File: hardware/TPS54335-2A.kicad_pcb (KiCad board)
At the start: 2 copper layers, 17 parts, among them J1 header, U1 TPS54335-2A

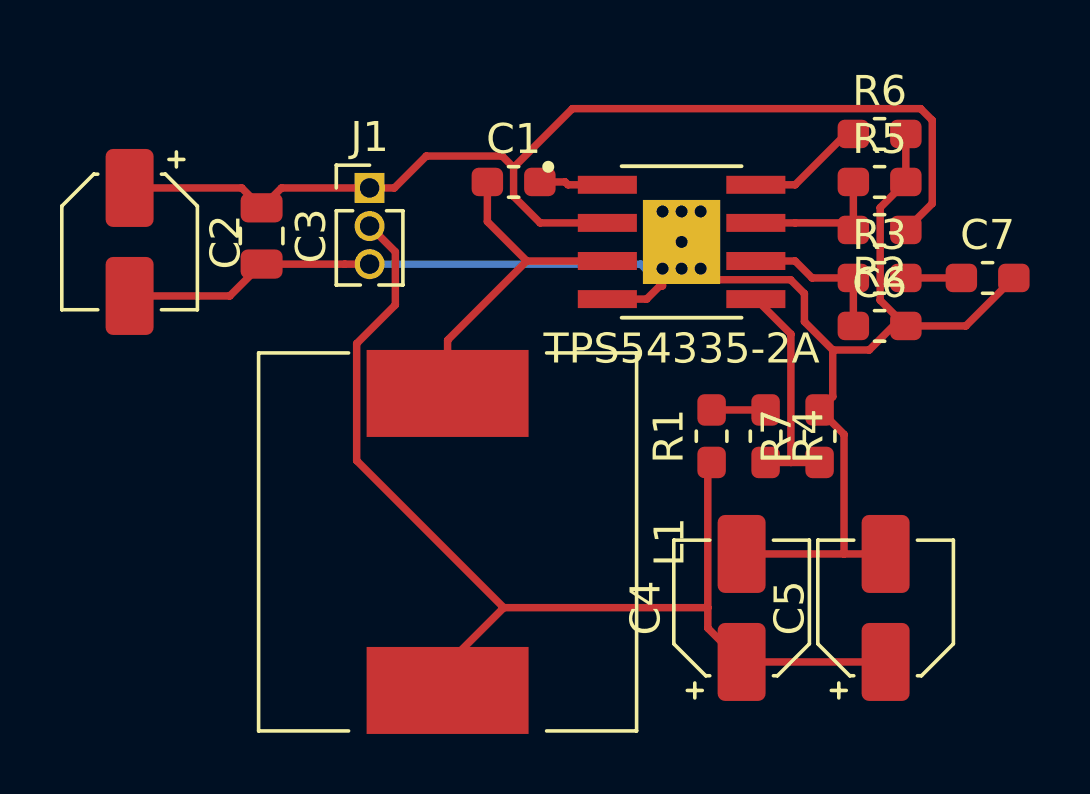
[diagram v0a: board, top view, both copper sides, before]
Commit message: update for track width,
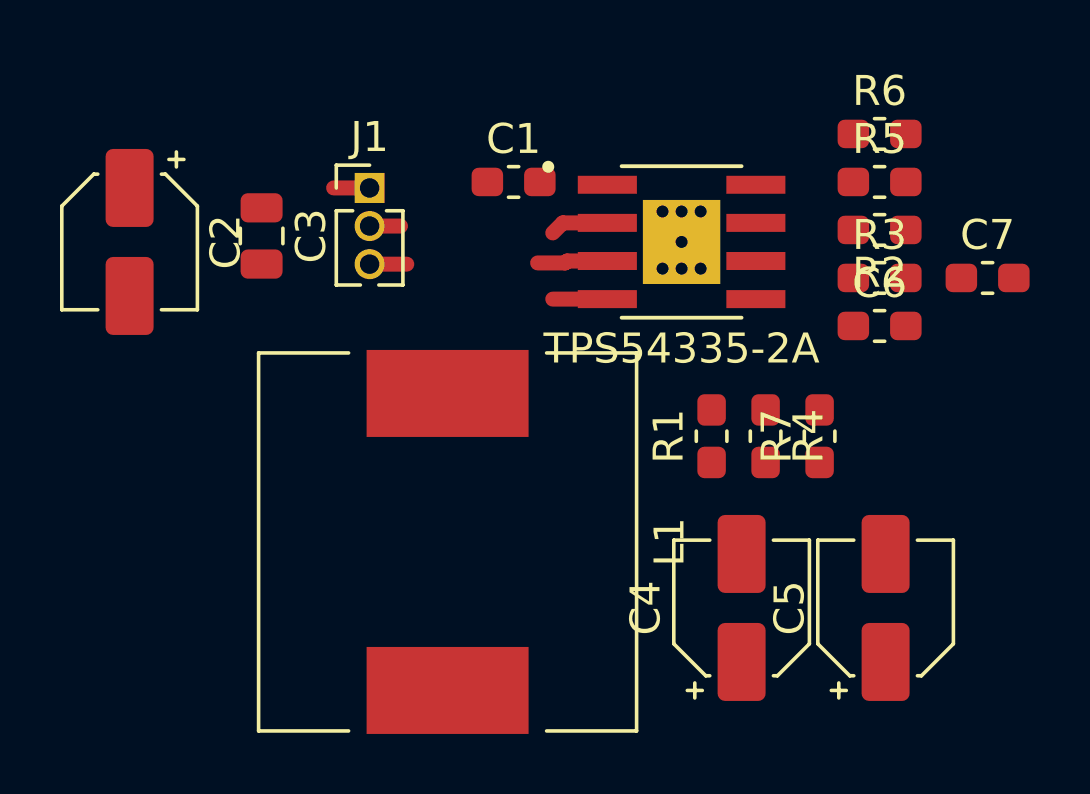
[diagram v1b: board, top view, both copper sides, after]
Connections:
- net Net-(C1-Pad1) renamed /PH_NET
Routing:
- net GND: track 57.5 -> 3.06 mm
- net +5V: track 37.9 -> 1.03 mm
- net +12V: track 37.3 -> 3.16 mm
- net /PH_NET: track 11.4 -> 2.35 mm
- net /Vsense: track 7.73 -> 0.00 mm
- net Net-(C6-Pad1): track 5.08 -> 0.00 mm
- net Net-(R2-Pad2): track 4.85 -> 0.00 mm
- net Net-(R6-Pad1): track 3.95 -> 0.00 mm
- net Net-(C1-Pad2): track 2.29 -> 0.00 mm
- net Net-(C7-Pad1): track 1.85 -> 0.00 mm
- net Net-(R1-Pad2): track 1.80 -> 0.00 mm
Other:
- net class 1A added: clearance 0.2, trace_width 0.75, via_dia 0.8, via_drill 0.4
- net class 3A added: clearance 0.5, trace_width 1.25, via_dia 0.8, via_drill 0.4
- net class GND added: clearance 0.2, trace_width 1.5, via_dia 0.8, via_drill 0.4

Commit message: update routing,
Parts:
- moved C5 25.7 mm to (52.7, 43.7)
- moved C7 25.7 mm to (56.1, 32.7)
- moved L1 25.7 mm to (38.1, 41.5)
- moved R4 25.7 mm to (48.7, 38.0)
- moved C1 25.7 mm to (40.3, 29.5)
- moved C2 25.7 mm to (27.5, 31.5)
- moved C3 25.7 mm to (31.9, 31.3)
- moved C4 25.7 mm to (47.9, 43.7)
- moved J1 25.7 mm to (35.5, 29.7)
- moved R1 25.7 mm to (46.9, 38.0)
- moved R2 25.7 mm to (52.5, 31.1)
- moved R3 25.7 mm to (52.5, 32.7)
- moved R5 25.7 mm to (52.5, 29.5)
- moved R6 25.7 mm to (52.5, 27.9)
- moved R7 25.7 mm to (50.5, 38.0)
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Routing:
- net GND: track 3.06 -> 96.9 mm, vias 0 -> 1
- net +5V: track 1.03 -> 43.2 mm, vias 0 -> 2
- net +12V: track 3.16 -> 18.5 mm, vias 0 -> 1
- net /Vsense: track 0.00 -> 10.5 mm
- net /PH_NET: track 2.35 -> 11.6 mm
- net Net-(C6-Pad1): track 0.00 -> 5.08 mm
- net Net-(R2-Pad2): track 0.00 -> 4.95 mm
- net Net-(R6-Pad1): track 0.00 -> 3.95 mm
- net Net-(C1-Pad2): track 0.00 -> 2.29 mm
- net Net-(C7-Pad1): track 0.00 -> 1.85 mm
- net Net-(R1-Pad2): track 0.00 -> 1.80 mm
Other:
- board outline added: 45 x 25 mm
